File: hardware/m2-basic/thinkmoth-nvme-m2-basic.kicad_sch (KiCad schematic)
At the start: 25 parts, among them J2 ExpressCard, J3 MDT180M03001

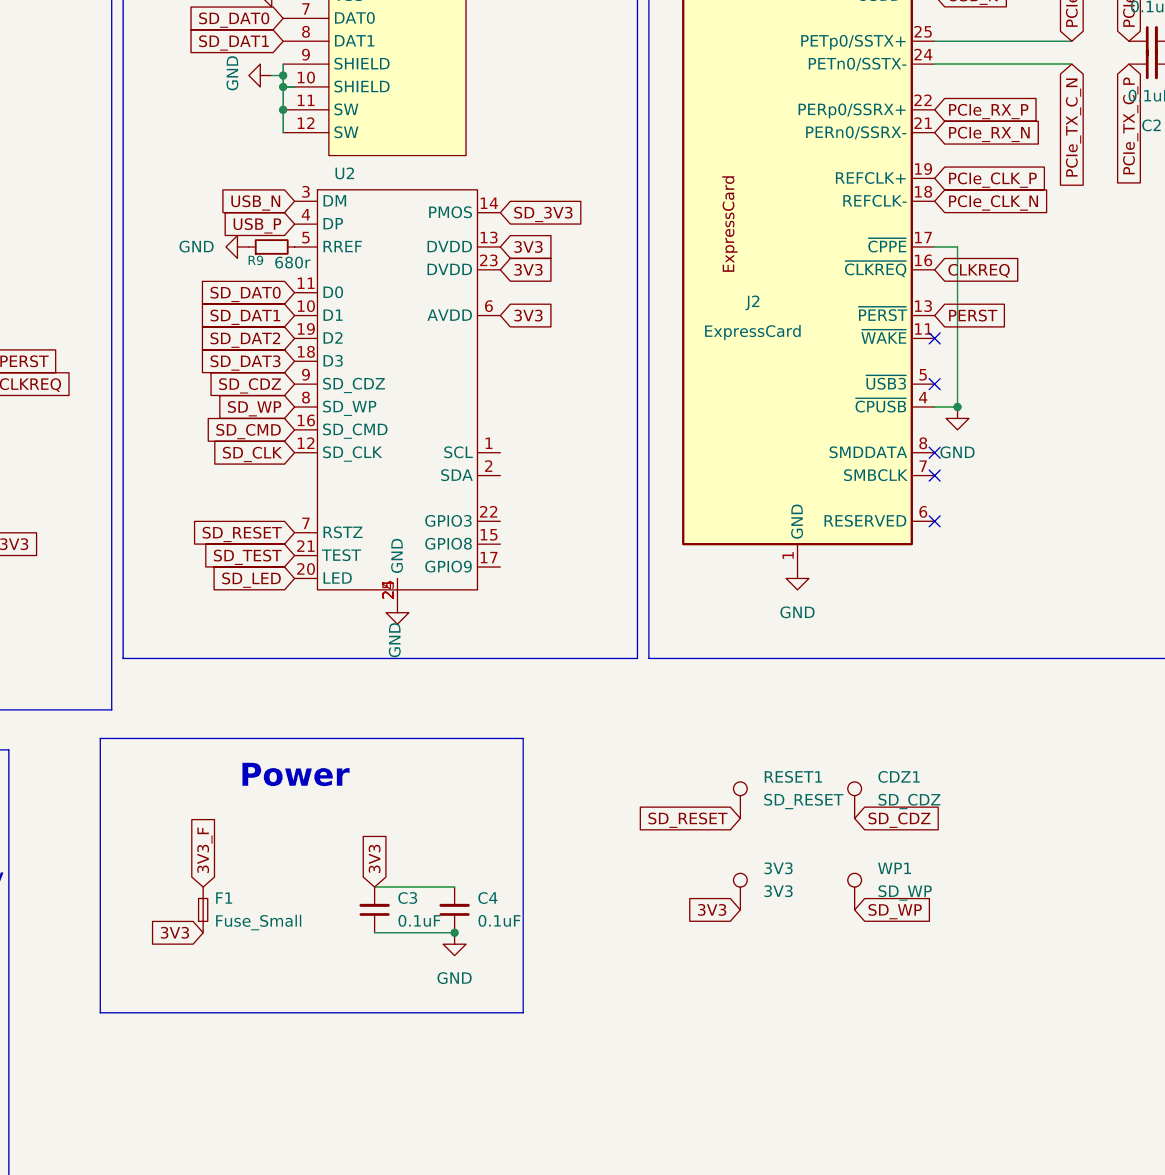
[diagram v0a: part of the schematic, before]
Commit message: m.2-basic: updated layout, moved mounting holes
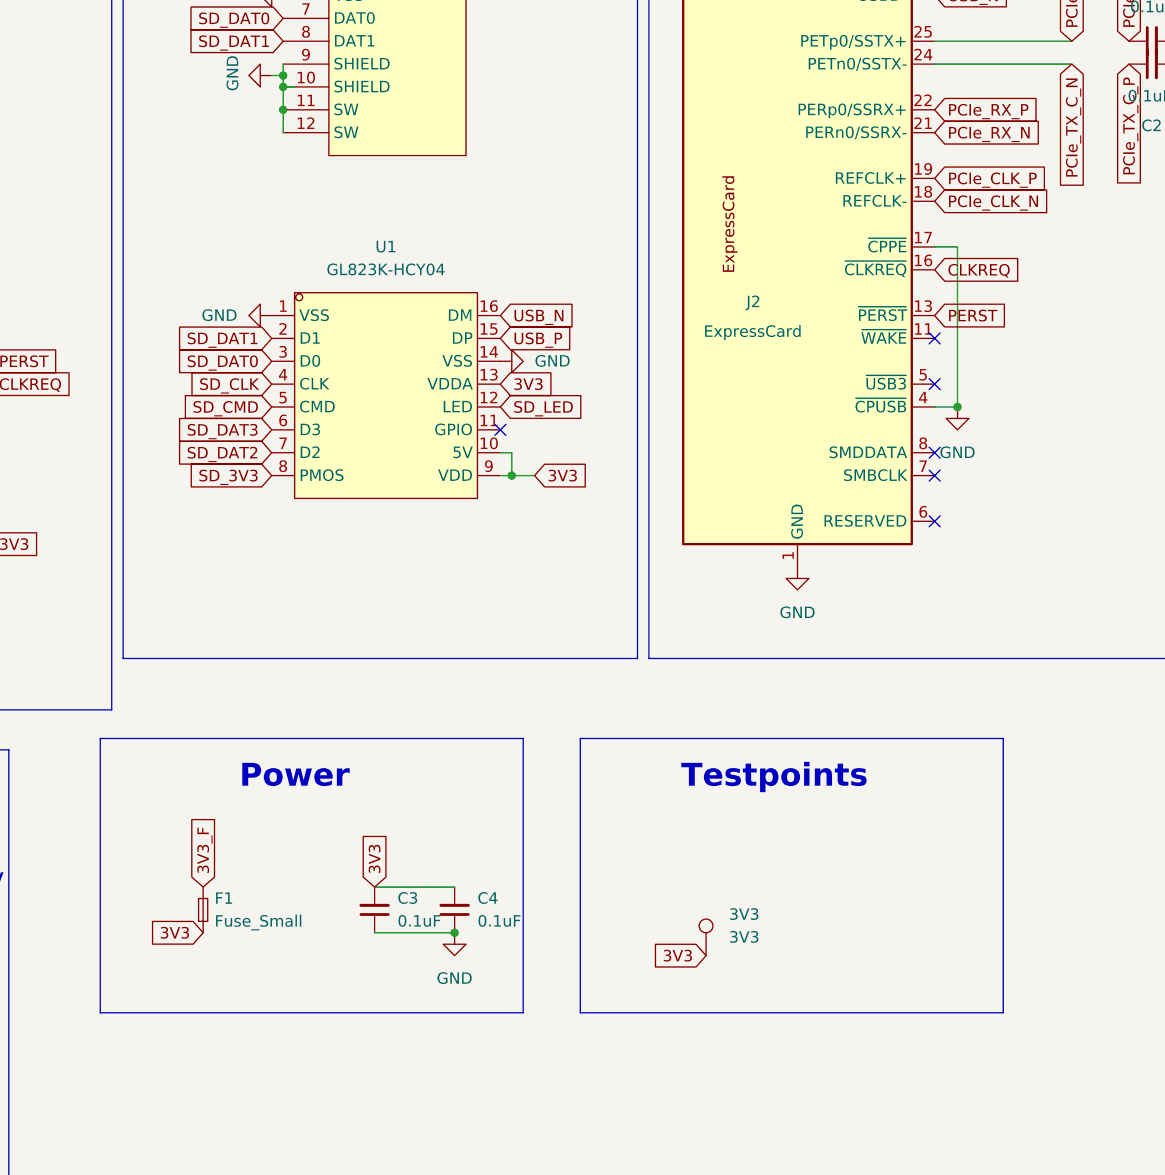
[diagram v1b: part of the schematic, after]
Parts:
- removed CDZ1: SD_CDZ, TestPoint:TestPoint_Pad_D1.0mm, symbol Connector:TestPoint
- removed R9: 680r, Resistor_SMD:R_0402_1005Metric, symbol Device:R_Small
- removed RESET1: SD_RESET, TestPoint:TestPoint_Pad_D1.0mm, symbol Connector:TestPoint
- removed U2: ~, Package_DFN_QFN:QFN-24-1EP_4x4mm_P0.5mm_EP2.7x2.6mm_ThermalVias, symbol GL823-B-QFN24:GL823A
- removed WP1: SD_WP, TestPoint:TestPoint_Pad_D1.0mm, symbol Connector:TestPoint
- added U1: GL823K-HCY04, GL823K-HCY04:SSOP-16_L4.9-W3.9-P0.64-LS6.0-BL, symbol GL823K-HCY04:GL823K-HCY04
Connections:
- net 3V3: now also U1.10 (5V), U1.13 (VDDA), U1.9 (VDD)
- net GND: now also U1.1 (VSS), U1.14 (VSS)
- net SD_3V3: now also U1.8 (PMOS)
- net SD_CLK: now also U1.4 (CLK)
- net SD_CMD: now also U1.5 (CMD)
- net SD_DAT0: now also U1.3 (D0)
- net SD_DAT1: now also U1.2 (D1)
- net SD_DAT2: now also U1.7 (D2)
- net SD_DAT3: now also U1.6 (D3)
- net SD_LED: now also U1.12 (LED)
- net USB_N: now also U1.16 (DM)
- net USB_P: now also U1.15 (DP)
- no-connect marks 42 -> 43
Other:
- note added: "Testpoints"
- moved on the sheet: 3V3

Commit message: m.2-basic: schematic clean up
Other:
- note added: "A cool open source ExpressCard to NVMe SSD adapter Supports both M.2 2230 and M.2242, and supports booting via a microSD card This board doesn't support SATA :("
- note removed: "An adapter to connect an M.2 NVMe SSD to an ExpressCard34/54 port"
- note removed: "M.2 version - M.2 2242 [*] - M.2 2230 [ ]"
- title: ThinkMoth M.2 2242 -> ThinkMoth NVMe
- moved on the sheet: 3V3, J3

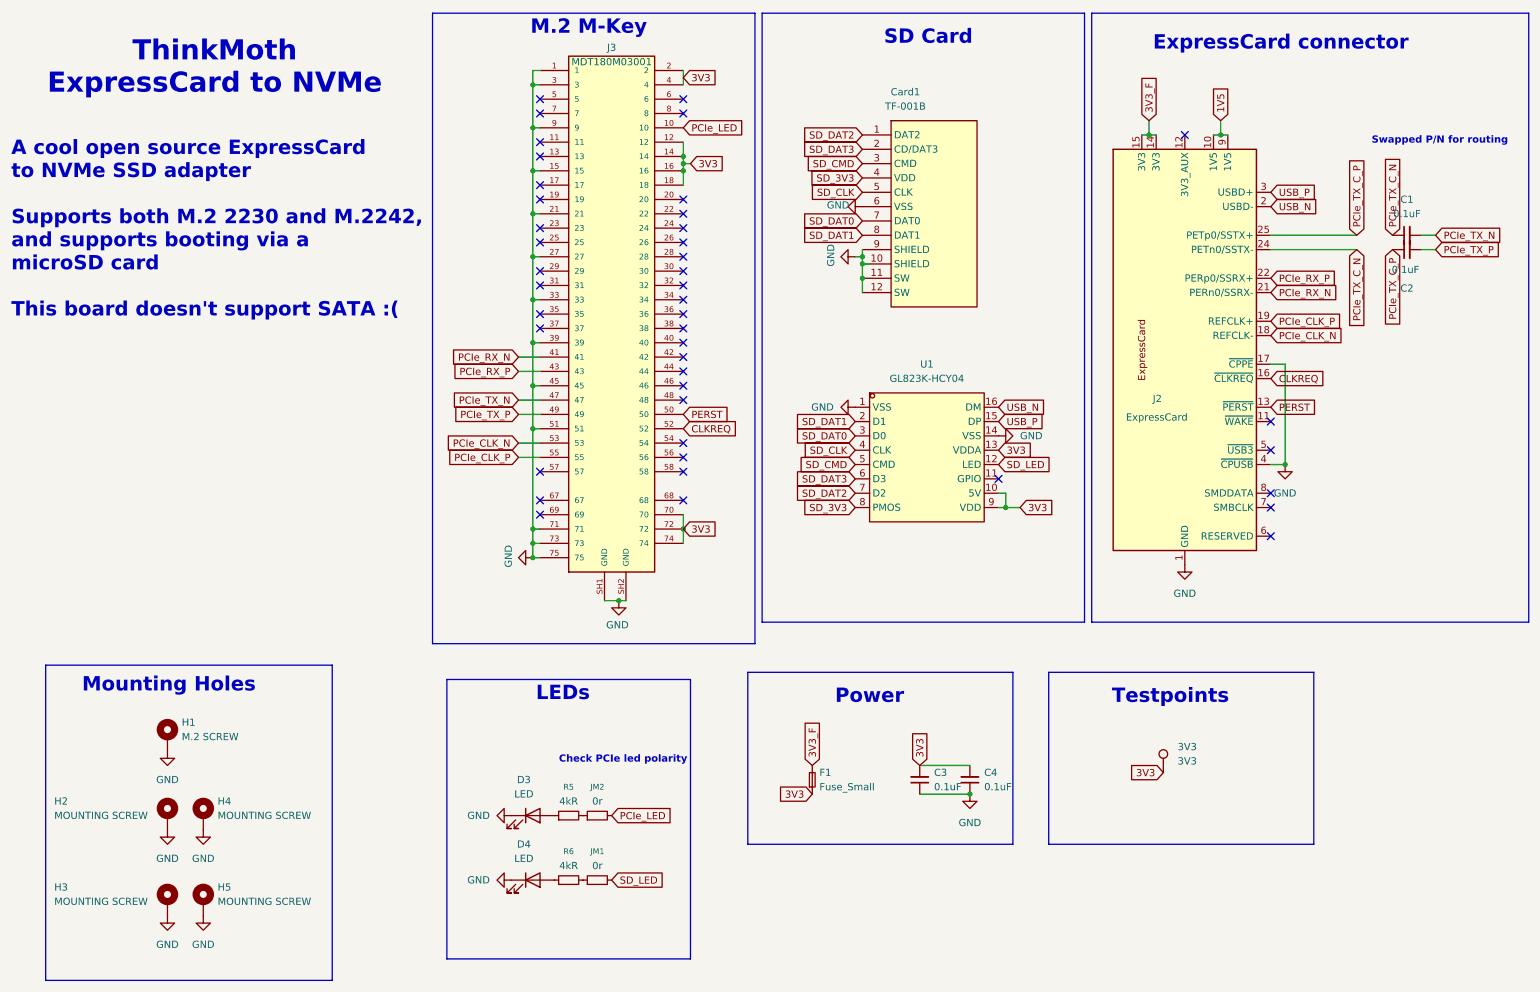
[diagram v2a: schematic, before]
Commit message: m.2-basic: minor layout tweaks, schem update
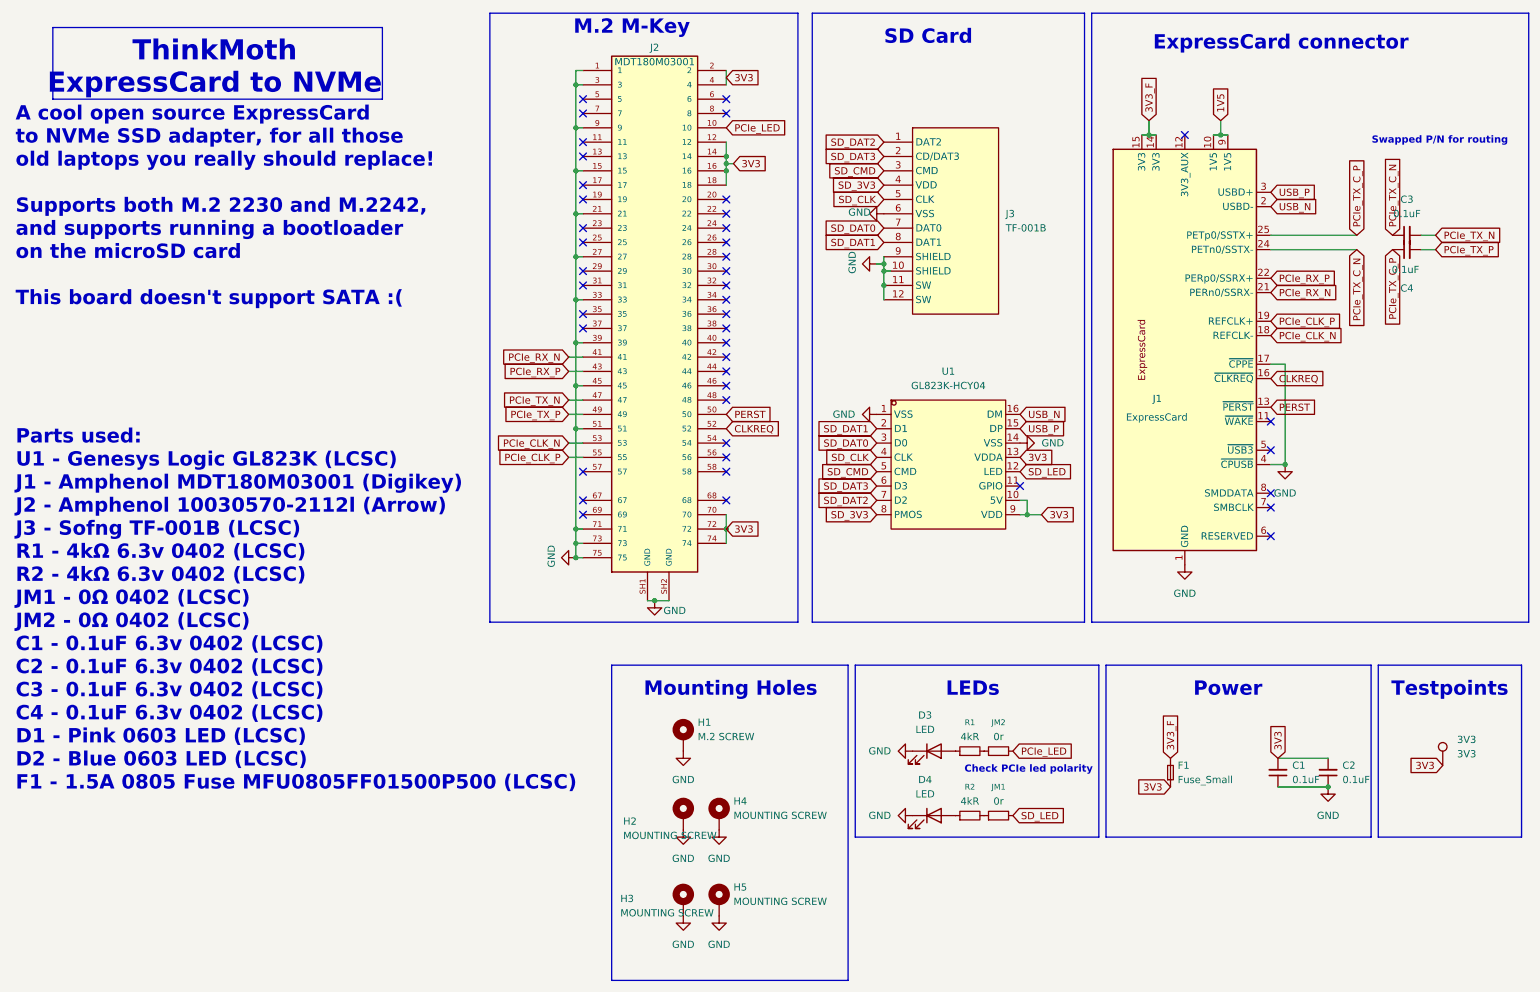
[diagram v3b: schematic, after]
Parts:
- renumbered C3 to C1, C4 to C2, C1 to C3, C2 to C4, J2 to J1, J3 to J2, Card1 to J3, R5 to R1, R6 to R2
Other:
- note added: "A cool open source ExpressCard to NVMe SSD adapter, for all those old laptops you really should replace! Supports both M.2 2230 and M.2242, and supports running a bootloader on the microSD card This board doesn't support SATA :( Parts used: U1 - Genesys Logic GL823K (LCSC) J1 - Amphenol MDT180M03001 (Digikey) J2 - Amphenol 10030570-2112l (Arrow) J3 - Sofng TF-001B (LCSC) R1 - 4kΩ 6.3v 0402 (LCSC)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"
- note removed: "A cool open source ExpressCard to NVMe SSD adapter Supports both M.2 2230 and M.2242, and supports booting via a microSD card This board doesn't support SATA :("
- moved on the sheet: 3V3, C1, C2, D3, D4, F1, H1, H2, H3, H4, H5, J2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

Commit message: updates for prototype run
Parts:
- J2: footprint MDT180M03001:AMPHENOL_MDT180M03001 -> thinkmoth:AMPHENOL_MDT180M03001
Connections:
- net PCIe_LED renamed LED_PCIe
- net SD_LED renamed LED_SD
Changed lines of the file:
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@@
 		)
 	)
-	(global_label "SD_LED"
+	(global_label "LED_SD"
 		(shape input)
 		(at 193.04 95.25 0)
@@
 		)
 	)
-	(global_label "PCIe_LED"
+	(global_label "LED_PCIe"
 		(shape input)
 		(at 140.97 34.29 0)
@@
 		)
 	)
-	(global_label "PCIe_LED"
+	(global_label "LED_PCIe"
 		(shape input)
 		(at 191.77 144.78 0)
@@
 		)
 	)
-	(global_label "SD_LED"
+	(global_label "LED_SD"
 		(shape input)
 		(at 191.77 156.21 0)
@@
 			)
 		)
-		(property "Footprint" "MDT180M03001:AMPHENOL_MDT180M03001"
+		(property "Footprint" "thinkmoth:AMPHENOL_MDT180M03001"
 			(at 128.27 67.31 0)
 			(effects

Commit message: minor tweaks
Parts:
- removed J3: TF-001B, SOFNG-TF-001B:TF-SMD_TF-001B, symbol SOFNG-TF-001B:TF-001B
- added J3: TF-009, SOFNG-TF-009:TF-SMD_TF-009, symbol SOFNG-TF-009:TF-009
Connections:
- net GND: now also J3.6 (VSS), J3.9 (EH)
- net SD_3V3: now also J3.4 (VDD)
- net SD_CLK: now also J3.5 (CLK)
- net SD_CMD: now also J3.3 (CMD)
- net SD_DAT0: now also J3.7 (DAT0)
- net SD_DAT1: now also J3.8 (DAT1)
- net SD_DAT2: now also J3.1 (DAT2)
- net SD_DAT3: now also J3.2 (CD/DAT3)
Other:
- note added: "An open source ExpressCard to NVMe adapter for old laptops :) Supports both M.2 2230 and M.2242, and supports running a bootloader on the microSD card This board doesn't support SATA :( Partlist: U1 - Genesys Logic GL823K (LCSC) J1 - Amphenol 10030570-2112l (Arrow) J2 - Amphenol MDT180M03001 (Digikey) J3 - Sofng TF-001B (LCSC) R1 - 4kΩ 6.3v 0402 (LCSC) R2 - 4kΩ 6.3v 0402 (LCSC) JM1 - 0Ω 0402 (LCS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"
- note removed: "A cool open source ExpressCard to NVMe SSD adapter, for all those old laptops you really should replace! Supports both M.2 2230 and M.2242, and supports running a bootloader on the microSD card This board doesn't support SATA :( Parts used: U1 - Genesys Logic GL823K (LCSC) J1 - Amphenol MDT180M03001 (Digikey) J2 - Amphenol 10030570-2112l (Arrow) J3 - Sofng TF-001B (LCSC) R1 - 4kΩ 6.3v 0402 (LCSC)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"
